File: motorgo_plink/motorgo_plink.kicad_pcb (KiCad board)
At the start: 4 copper layers, 80.5 x 64.5 mm, 141 parts, among them J1 USB4520-03-0-A_REVA, J10 Conn_01x02_Pin, J13 I2C_STANDARDQWIIC, J14 BM05B-SRSS-TB_LF__SN_, J15 I2C_STANDARDQWIIC, J16 BM05B-SRSS-TB_LF__SN_, J17 I2C_STANDARDQWIIC, J18 BM05B-SRSS-TB_LF__SN_, J19 I2C_STANDARDQWIIC, J20 BM05B-SRSS-TB_LF__SN_, J22 Conn_01x02_Pin, J23 Conn_01x06_Pin, J4 Conn_02x20_Odd_Even, J5 Conn_02x20_Odd_Even, J6 Conn_01x02_Pin, J7 USB4520-03-0-A_REVA, J8 Conn_01x02_Pin, Q1 SI2323, U1 ESP32-S3-WROOM-1, U10 LIS3MDLTR, U11 LSM6DS3TR, U2 USBLC6-2P6, U3 DRV8874PWPR, U4 DRV8874PWPR, U5 DRV8874PWPR, U6 TPS54620RHLR, U7 HUSB238_002DD, U8 AMS1117-3.3, U9 DRV8874PWPR

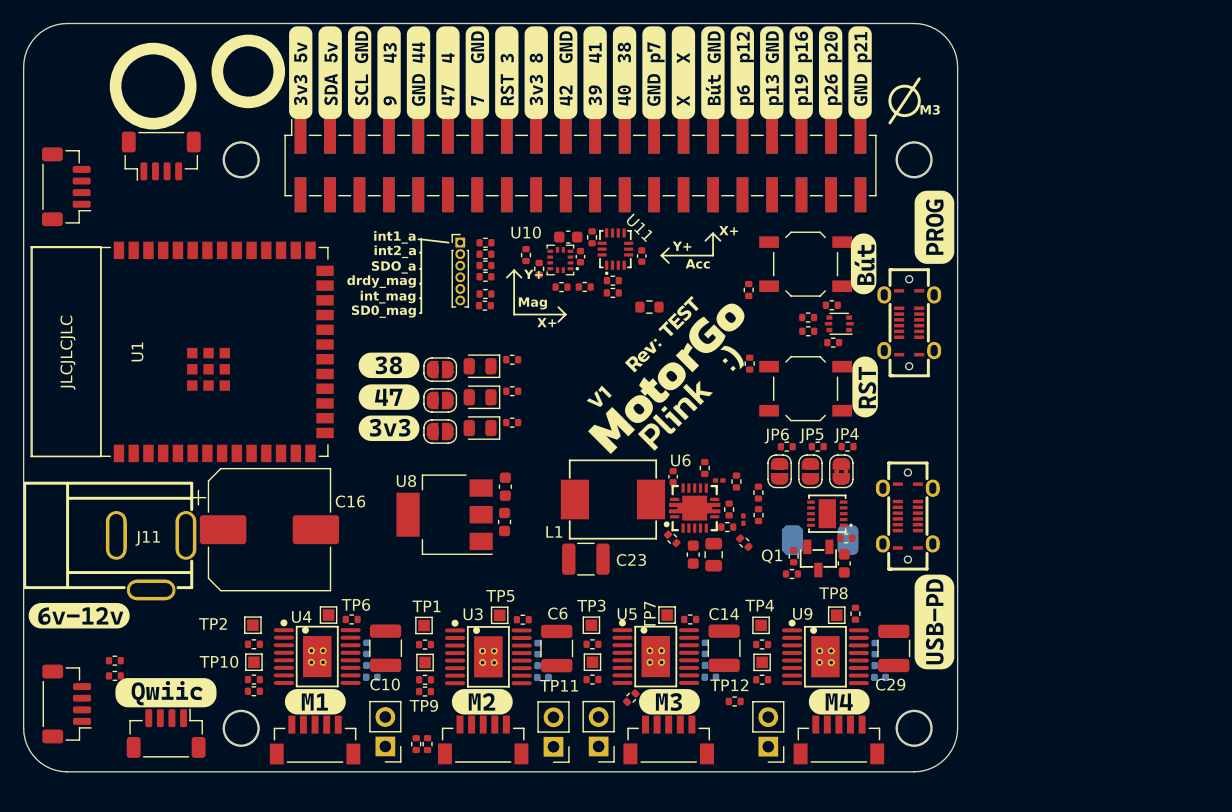
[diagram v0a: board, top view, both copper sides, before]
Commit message: wip layout work begun, board dimensions finalized
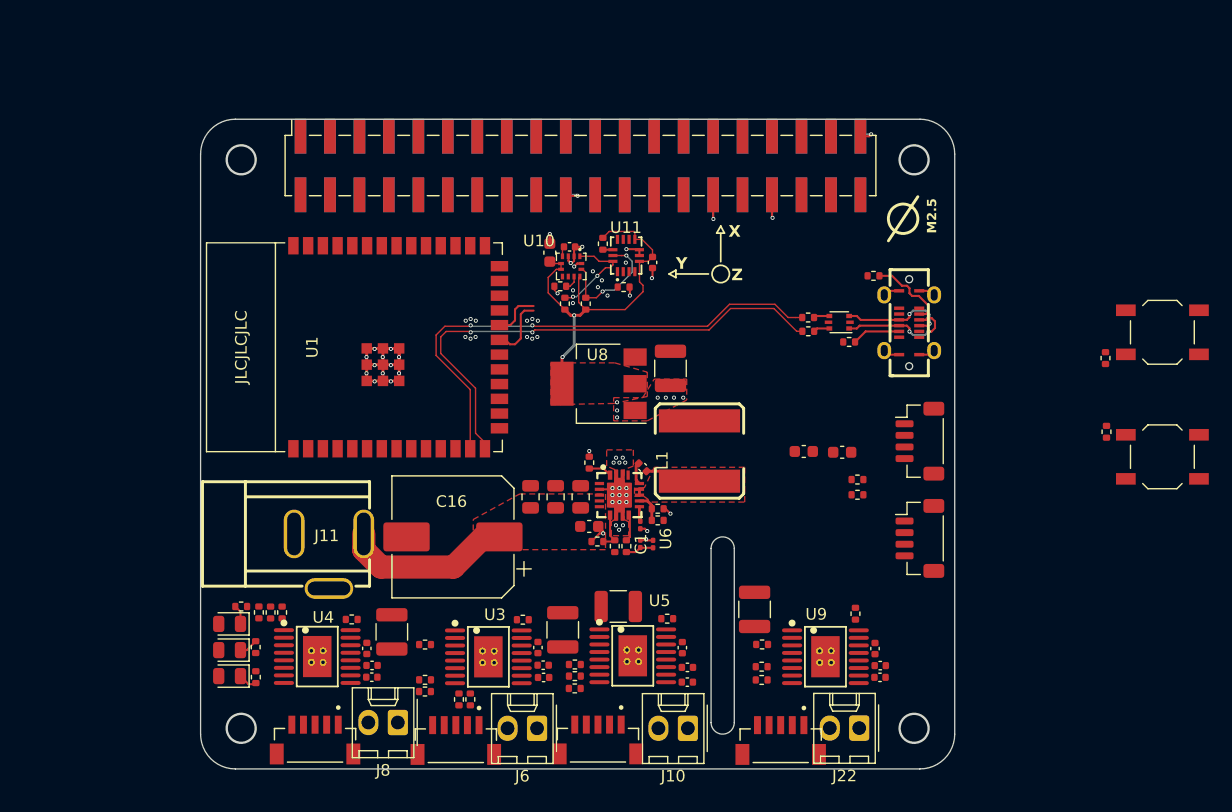
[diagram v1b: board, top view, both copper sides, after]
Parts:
- removed C21: 1uF, Capacitor_SMD:C_0603_1608Metric
- removed D4: 20V 5A, LCSC_parts:D_SMB_LCSC_C5366311
- removed J17, J19: I2C_STANDARDQWIIC, Connector_JST:JST_SH_BM04B-SRSS-TB_1x04-1MP_P1.00mm_Vertical
- removed J23: Conn_01x06_Pin, Connector_PinHeader_1.00mm:PinHeader_1x06_P1.00mm_Vertical
- removed J7: USB4520-03-0-A_REVA, mg_mini_v1r3:USB-C-SMD_TYPEC-303-ACP16
- removed JP1, JP2, JP3: DNP, Jumper:SolderJumper-2_P1.3mm_Open_RoundedPad1.0x1.5mm
- removed JP4: SolderJumper_2_Bridged, Jumper:SolderJumper-2_P1.3mm_Bridged2Bar_RoundedPad1.0x1.5mm
- removed JP5, JP6: SolderJumper_2_Open, Jumper:SolderJumper-2_P1.3mm_Open_RoundedPad1.0x1.5mm
- removed Q1: SI2323, LCSC_parts:SI2323_SOT-23-3_L2.9-W1.3-P0.95-LS2.4-BR
- removed R20: 10R 1%, Resistor_SMD:R_0402_1005Metric
- removed R21, R22, R40, R41, R42, R43, R44, R45, R47, R48: DNP, Resistor_SMD:R_0402_1005Metric
- removed R23: 5.1K, Resistor_SMD:R_0402_1005Metric
- removed R26: 49.9K, Resistor_SMD:R_0402_1005Metric
- removed R27: 10K, Resistor_SMD:R_0402_1005Metric
- removed R28: 14K, Resistor_SMD:R_0402_1005Metric
- removed R29: 10.5K, Resistor_SMD:R_0402_1005Metric
- removed R34: 0R0, Resistor_SMD:R_0603_1608Metric
- removed TP1, TP10, TP11, TP12, TP2, TP3, TP4, TP5, TP6, TP7, TP8, TP9: TestPoint, TestPoint:TestPoint_Pad_1.0x1.0mm
- removed U7: HUSB238_002DD, LCSC_parts:DFN-10_L3.0-W3.0-P0.50-BL-EP2.5
- added C1: 30pF 0Ohm, Capacitor_SMD:C_0201_0603Metric, F.Cu at (148.5, 96.6)
- added C19: 10uF 1mOhm, Capacitor_SMD:C_0805_2012Metric, F.Cu at (137.9, 92.5)
- added C2: 10uF 1mOhm, Capacitor_SMD:C_0805_2012Metric, F.Cu at (142.3, 92.5)
- C11, C12, C13, C26, C27, C28, C3, C4, C5, C7, C8, C9: moved to F.Cu
- C15: value 10uF 4mOhm -> 10uF 1mOhm
- C20: value 43pF 0Ohm -> 16nF 0Ohm
- C23: value 47uF 1mOhm -> 47uF 3mOhm
- J10, J22, J6, J8: footprint Connector_PinHeader_2.54mm:PinHeader_1x02_P2.54mm_Vertical -> Connector_Molex:Molex_KK-254_AE-6410-02A_1x02_P2.54mm_Vertical
- L1: value 3.3uH 14mOhm -> 3.3uH 14.3mOhm; footprint LCSC_parts:IND-SMD_L7.3-W6.6 -> kicad_lceda:IND-SMD_L6.6-W6.4_CKSTT0610
- R19: value 3.4k -> 4.02k
- R24: value 52.3k -> 53.6k
- moved J15 79.6 mm to (171.5, 96.1), turned to -90 degrees
- moved J13 69.9 mm to (171.5, 87.8), turned to -90 degrees
- moved R31 66.2 mm to (166.1, 91.1), turned to 0 degrees
- moved R30 65.6 mm to (166.1, 92.4), turned to 0 degrees
- moved R2 31.6 mm to (113.0, 102.0)
- moved J2 31.3 mm to (192.4, 78.4)
- moved J3 31.3 mm to (192.4, 89.1)
- moved R9 31.3 mm to (187.6, 86.9)
- moved R8 31.3 mm to (187.5, 80.6)
- moved R1 31.2 mm to (114.2, 105.5), turned to -90 degrees
- moved R3 31.1 mm to (114.3, 108.1), turned to 90 degrees
- moved D2 31.0 mm to (112.0, 103.5)
- moved D1 30.7 mm to (112.0, 105.8)
- moved D3 30.4 mm to (112.0, 108.0)
- moved C24 29.2 mm to (164.8, 88.7), turned to 180 degrees
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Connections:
- net /IMU 6 + 3/SDO_acc renamed Net-(U11-SDO/SA0)
- net /IMU 6 + 3/SDO_mag renamed Net-(U10-SD0/SA1)
- net enc_scl renamed /connectors.enc_scl
- net enc_sda renamed /connectors.enc_sda
- net m1_enc_cs renamed /connectors.enc1.cs
- net m2_enc_cs renamed /connectors.enc2.cs
- net m3_enc_cs renamed /connectors.enc3.cs
- net m4_enc_cs renamed /connectors.enc4.cs
- C30 pad 1: GNDD -> GND
- C31 pad 2: GNDD -> GND
- C32 pad 2: GNDD -> GND
- D1 pad 2: Net-(D1-A) -> gpio42
- D2 pad 2: Net-(D2-A) -> /gpio21
- D3 pad 2: Net-(D3-A) -> +3.3V
- J2 pad 2: boot -> /Boot
- J4 pad 15: Reset -> reset
- J4 pad 29: boot -> /Boot
- J5 pad 16: Reset -> reset
- R38 pad 2: hidden_sda -> /IMU 6 + 3/SDA_acc
- R39 pad 2: hidden_scl -> /IMU 6 + 3/SCL_acc
- R46 pad 2: GNDD -> GND
- R49 pad 2: GNDD -> GND
- R8 pad 2: boot -> /Boot
- U1 pad 21: hidden_sda -> /i2c_1.sda
- U1 pad 22: hidden_scl -> /i2c_1.scl
- U1 pad 23: gpio38 -> /gpio21
- U1 pad 24: gpio41 -> gpio47
- U1 pad 25: gpio42 -> gpio48
- U1 pad 27: boot -> /Boot
- U1 pad 28: gpio4 -> gpio35
- U1 pad 29: gpio7 -> gpio36
- U1 pad 30: gpio3 -> gpio37
- U1 pad 31: gpio8 -> gpio38
- U1 pad 34: gpio44 -> gpio41
- U1 pad 35: gpio47 -> gpio42
- U1 pad 36: gpio43 -> gpio44
- U1 pad 37: gpio9 -> gpio43
- U10 pad 1: hidden_scl -> /IMU 6 + 3/SCL_acc
- U10 pad 11: hidden_sda -> /IMU 6 + 3/SDA_acc
- U10 pad 12: GNDD -> GND
- U10 pad 2: GNDD -> GND
- U10 pad 3: GNDD -> GND
- U10 pad 7: /IMU 6 + 3/INT_mag -> unconnected-(U10-INT-Pad7)
- U10 pad 8: /IMU 6 + 3/DRDY_mag -> unconnected-(U10-DRDY-Pad8)
- U11 pad 13: hidden_sda -> /IMU 6 + 3/SDA_acc
- U11 pad 14: hidden_scl -> /IMU 6 + 3/SCL_acc
- U11 pad 2: /IMU 6 + 3/SDX_acc -> unconnected-(U11-SDX-Pad2)
- U11 pad 3: /IMU 6 + 3/SCX_acc -> unconnected-(U11-SCX-Pad3)
- U11 pad 4: /IMU 6 + 3/INT1_acc -> unconnected-(U11-INT1-Pad4)
- U11 pad 6: GNDD -> GND
- U11 pad 7: GNDD -> GND
- U11 pad 9: /IMU 6 + 3/INT2_acc -> unconnected-(U11-INT2-Pad9)
- U3 pad 3: Net-(U3-nSLEEP) -> Net-(U3-nFAULT)
- U4 pad 3: Net-(U4-nSLEEP) -> Net-(U4-nFAULT)
- U5 pad 3: Net-(U5-nSLEEP) -> Net-(U5-nFAULT)
- U9 pad 3: Net-(U9-nSLEEP) -> Net-(U9-nFAULT)
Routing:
- net GND: track 0.00 -> 52.0 mm, vias 0 -> 72
- net usb_d+: track 0.00 -> 44.3 mm, vias 0 -> 2
- net usb_d-: track 0.00 -> 44.3 mm, vias 0 -> 2
- net +3.3V: track 0.00 -> 33.7 mm, vias 0 -> 2
- net +BATT: track 0.00 -> 14.8 mm
- net /IMU 6 + 3/SDA_acc: track 0.00 -> 10.4 mm, vias 0 -> 2
- net Net-(J1-DP1): track 0.00 -> 10.4 mm, vias 0 -> 2
- net Net-(J1-DN1): track 0.00 -> 9.46 mm, vias 0 -> 2
- net /IMU 6 + 3/SCL_acc: track 0.00 -> 8.65 mm, vias 0 -> 2
- net Net-(J1-CC2): track 0.00 -> 6.90 mm
- net /i2c_1.sda: track 0.00 -> 5.53 mm
- net Net-(C22-Pad1): track 0.00 -> 5.42 mm
- net Net-(J1-CC1): track 0.00 -> 4.18 mm
- net /i2c_1.scl: track 0.00 -> 4.18 mm
- net Net-(U6-VSENSE): track 0.00 -> 3.37 mm
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- added copper zone on F.Cu, net +3.3V
- added copper zone on F.Cu, net +BATT
- added copper zone on F.Cu, net GND
- added copper zone on In1.Cu, net GND
- added copper zone on In2.Cu, net GND
- added copper zone on F.Cu, net Net-(C22-Pad1)
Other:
- board size 80.5 x 64.5 mm -> 65 x 56 mm
- board text added: "M2.5"
- board text added: "R = 3mm"
- board text added: "X"
- board text added: "Y"
- board text added: "Z"
- board text removed: "Acc"
- board text removed: "M3"
- board text removed: "Mag"
- board text removed: "X+"
- board text removed: "Y+"
- board text removed: "int1_a SDO_a int_mag"
- board text removed: "int2_a drdy_mag SD0_mag"

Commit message: layout complete! checkpoint ready for design review
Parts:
- removed J5: Conn_02x20_Odd_Even, Connector_PinSocket_2.54mm:PinSocket_2x20_P2.54mm_Vertical_SMD
- added J7: Conn_02x20_Odd_Even, Connector_PinSocket_2.54mm:PinSocket_2x20_P2.54mm_Vertical_SMD, B.Cu at (142.2, 64.0)
- moved R32 30.9 mm to (162.7, 110.7), turned to 0 degrees
- moved J2 29.2 mm to (164.5, 87.0), turned to -90 degrees
- moved R33 28.0 mm to (160.7, 110.7), turned to 0 degrees
- moved R8 24.4 mm to (165.9, 91.9), turned to 180 degrees
- moved C25 23.1 mm to (138.6, 85.4), turned to -90 degrees
- moved J3 21.8 mm to (170.7, 87.0), turned to -90 degrees
- moved R9 20.3 mm to (167.9, 91.9), turned to 0 degrees
- moved C24 18.1 mm to (149.1, 79.7), turned to 90 degrees
- moved C26 14.3 mm to (159.6, 95.5), turned to 0 degrees
- moved C27 14.2 mm to (161.5, 95.6)
- moved C28 14.1 mm to (157.8, 95.5), turned to 0 degrees
- moved R37 11.7 mm to (156.2, 96.1)
- moved C31 10.9 mm to (159.4, 71.4)
- moved C32 10.9 mm to (150.5, 70.6)
- moved R38 10.9 mm to (153.6, 75.0)
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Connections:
- D1 pad 2: gpio42 -> gpio44
- D2 pad 2: /gpio21 -> gpio43
- J13 pad MP: (no net) -> GND
- J15 pad MP: (no net) -> GND
- J2 pad 2: /Boot -> boot
- J4 pad 1: +3.3V -> +5V
- J4 pad 10: gpio44 -> GND
- J4 pad 11: gpio47 -> gpio41
- J4 pad 12: gpio4 -> gpio39
- J4 pad 13: gpio7 -> GND
- J4 pad 14: GND -> gpio37
- J4 pad 15: reset -> gpio40
- J4 pad 16: gpio3 -> reset
- J4 pad 17: +3.3V -> gpio38
- J4 pad 18: gpio8 -> +3.3V
- J4 pad 19: gpio42 -> GND
- J4 pad 2: +5V -> +3.3V
- J4 pad 20: GND -> gpio35
- J4 pad 21: gpio39 -> gpio36
- J4 pad 22: gpio41 -> gpio48
- J4 pad 23: gpio40 -> gpio21
- J4 pad 24: gpio38 -> gpio47
- J4 pad 25: GND -> p26
- J4 pad 26: p26 -> GND
- J4 pad 29: /Boot -> GND
- J4 pad 3: sda -> +5V
- J4 pad 30: GND -> boot
- J4 pad 31: p31 -> p32
- J4 pad 32: p32 -> p31
- J4 pad 33: p33 -> GND
- J4 pad 34: GND -> p33
- J4 pad 35: p35 -> p36
- J4 pad 36: p36 -> p35
- J4 pad 37: p37 -> p38
- J4 pad 38: p38 -> p37
- J4 pad 39: GND -> p40
- J4 pad 4: +5V -> sda
- J4 pad 40: p40 -> GND
- J4 pad 5: scl -> GND
- J4 pad 6: GND -> scl
- J4 pad 7: gpio9 -> gpio43
- J4 pad 8: gpio43 -> gpio44
- J4 pad 9: GND -> gpio42
- R38 pad 2: /IMU 6 + 3/SDA_acc -> /i2c_1.sda
- R39 pad 2: /IMU 6 + 3/SCL_acc -> /i2c_1.scl
- R8 pad 2: /Boot -> boot
- U1 pad 10: m2_PH -> m2_EN
- U1 pad 11: m2_EN -> m2_PH
- U1 pad 12: m3_PH -> m3_EN
- U1 pad 15: m3_EN -> m3_PH
- U1 pad 17: /connectors.enc3.cs -> /connectors.enc4.cs
- U1 pad 18: m4_PH -> /connectors.enc3.cs
- U1 pad 20: /connectors.enc4.cs -> m4_PH
- U1 pad 23: /gpio21 -> gpio21
- U1 pad 27: /Boot -> boot
- U1 pad 38: sda -> scl
- U1 pad 39: scl -> sda
- U1 pad 4: /connectors.enc2.cs -> /connectors.enc1.cs
- U1 pad 5: /connectors.enc1.cs -> /connectors.enc2.cs
- U10 pad 1: /IMU 6 + 3/SCL_acc -> /i2c_1.scl
- U10 pad 11: /IMU 6 + 3/SDA_acc -> /i2c_1.sda
- U11 pad 13: /IMU 6 + 3/SDA_acc -> /i2c_1.sda
- U11 pad 14: /IMU 6 + 3/SCL_acc -> /i2c_1.scl
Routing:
- net +3.3V: track 33.7 -> 283.1 mm, vias 2 -> 15
- net +5V: track 0.00 -> 174.4 mm, vias 0 -> 25
- net reset: track 0.00 -> 105.5 mm, vias 0 -> 5
- net scl: track 0.00 -> 91.8 mm, vias 0 -> 2
- net sda: track 0.00 -> 86.6 mm, vias 0 -> 3
- net /connectors.enc_scl: track 0.00 -> 76.4 mm, vias 0 -> 6
- net /connectors.enc_sda: track 0.00 -> 75.0 mm, vias 0 -> 6
- net /connectors.enc3.cs: track 0.00 -> 66.7 mm, vias 0 -> 2
- net boot: track 0.00 -> 61.7 mm, vias 0 -> 2
- net /connectors.enc4.cs: track 0.00 -> 51.4 mm
- net gpio43: track 0.00 -> 50.1 mm, vias 0 -> 3
- net gpio44: track 0.00 -> 47.8 mm, vias 0 -> 3
- net +BATT: track 14.8 -> 61.6 mm
- net GND: track 52.0 -> 97.7 mm, vias 72 -> 201
- net m4_PH: track 0.00 -> 40.6 mm, vias 0 -> 2
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- added copper zone on B.Cu, net +5V
- added copper zone on F.Cu, net +5V
- added copper zone on F.Cu, net /motor_controls1/motor_out1
- added copper zone on F.Cu, net /motor_controls1/motor_out2
- added copper zone on F.Cu, net /motor_controls2/motor_out1
- added copper zone on F.Cu, net /motor_controls2/motor_out2
- added copper zone on F.Cu, net /motor_controls3/motor_out1
- added copper zone on F.Cu, net /motor_controls3/motor_out2
- added copper zone on F.Cu, net /motor_controls4/motor_out1
- added copper zone on F.Cu, net /motor_controls4/motor_out2
